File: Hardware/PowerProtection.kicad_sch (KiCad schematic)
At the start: 17 parts, among them IC5 LM76202QPWPRQ1

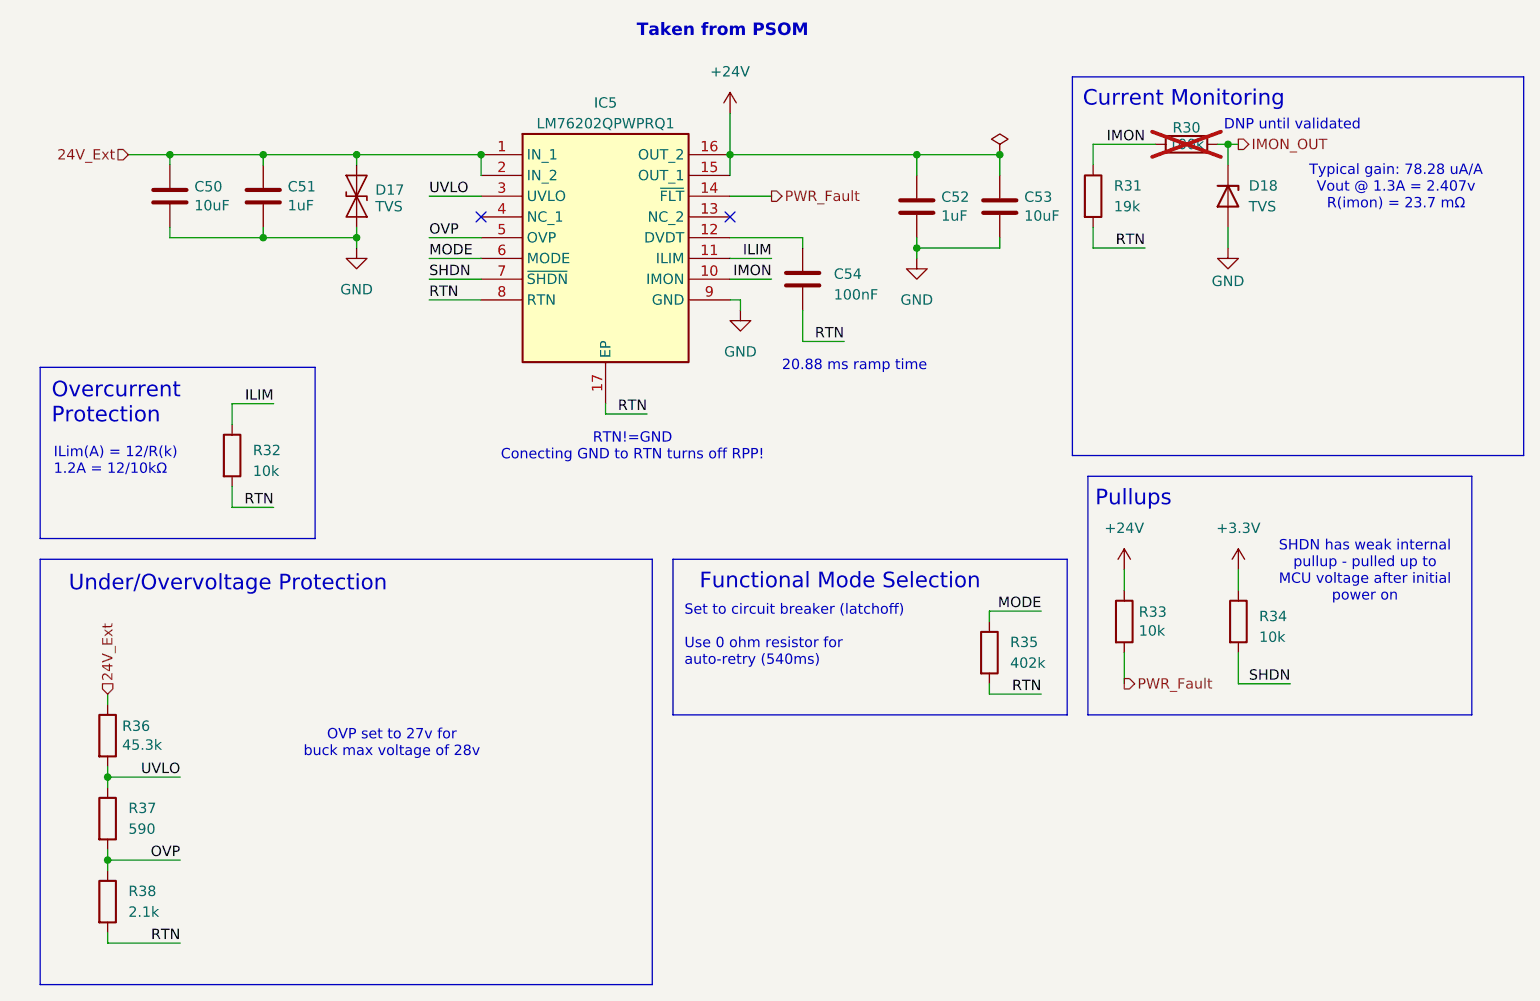
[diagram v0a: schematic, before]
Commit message: RevB Changes (#4)
* added documentation for current range; added VBUS led

* INA common-mode fixed (i think)

* differential amp for LPF

* diff amp / LPF

* some comments so I don't forget what I'm doing

* new TLV symbol, SPDT switch for scrut

* fixed LPF cutoff

* refactored and added LPF docs; added fuse, boot_gpio from USB-UART chip

* i lowk haven't started layout

* slightly cooked

* started layout not really but kind of

* layout stuff

* post review council sch changes: shielded connectors, removed SHDN resistor, diode OR for boot, standardized resistors

* starting routing i think

* almost done with routing

* wow

* drc is happy

* ye

* again

* addressed some comments

* added lcsc part numbers

* generated production files and docs

* updated STEP file

* symbol library

* addressed comments; generated production files, docs

* added Mouser BOM, deleted embedded step files
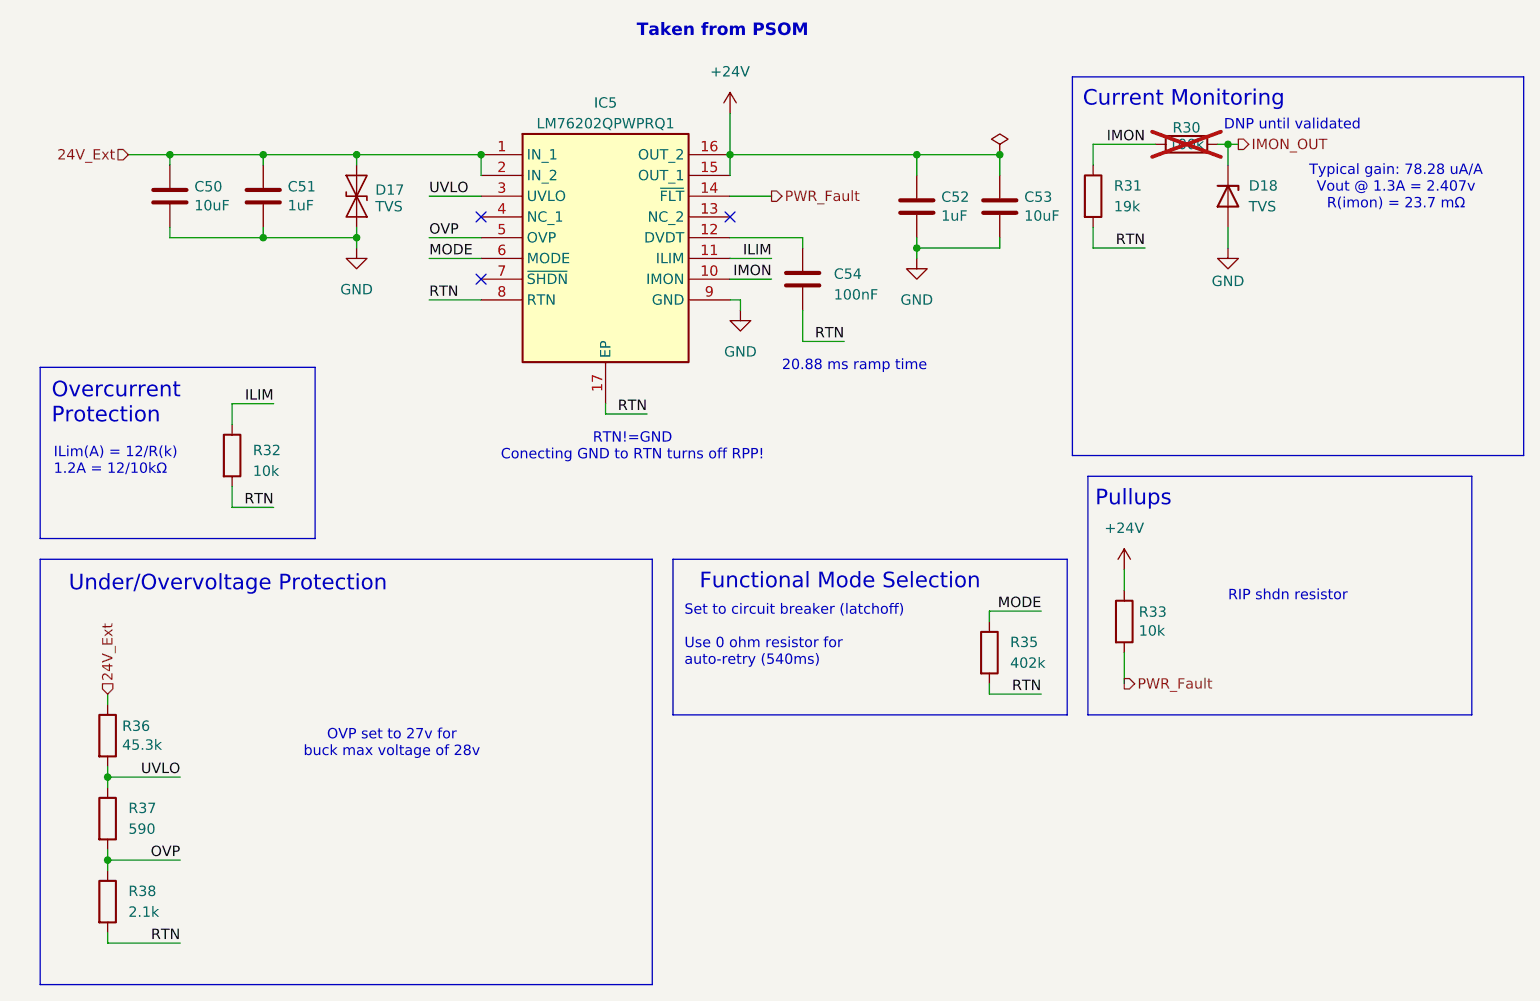
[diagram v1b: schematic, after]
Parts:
- removed R34: 10k, Resistor_SMD:R_0603_1608Metric_Pad0.98x0.95mm_HandSolder, symbol Device:R
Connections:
- net SHDN: no longer names the net of IC5.7 (~{SHDN})
- no-connect marks 2 -> 3
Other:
- note added: "RIP shdn resistor"
- note removed: "SHDN has weak internal pullup - pulled up to MCU voltage after initial power on"
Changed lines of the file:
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@@
 		)
 	)
+	(text "RIP shdn resistor"
+		(exclude_from_sim no)
+		(at 158.75 85.09 0)
+		(effects
+			(font
+				(size 1.27 1.27)
+			)
+			(justify left top)
+		)
+	)
 	(text "Under/Overvoltage Protection"
 		(exclude_from_sim no)
@@
 		)
 	)
-	(text "SHDN has weak internal\npullup - pulled up to\nMCU voltage after initial\npower on"
-		(exclude_from_sim no)
-		(at 175.514 82.804 0)
-		(effects
-			(font
-				(size 1.27 1.27)
-			)
-		)
-	)
 	(text "20.88 ms ramp time"
 		(exclude_from_sim no)
@@
 		(at 67.31 39.37)
 	)
+	(no_connect
+		(at 67.31 46.99)
+	)
 	(wire
 		(pts
@@
 	(wire
 		(pts
-			(xy 160.02 96.52) (xy 160.02 92.71)
-		)
-		(stroke
-			(width 0)
-			(type default)
-		)
-	)
-	(wire
-		(pts
 			(xy 36.83 62.23) (xy 36.83 64.77)
 		)
@@
 	(wire
 		(pts
-			(xy 166.37 96.52) (xy 160.02 96.52)
-		)
-		(stroke
-			(width 0)
-			(type default)
-		)
-	)
-	(wire
-		(pts
 			(xy 52.07 41.91) (xy 52.07 43.18)
 		)
@@
 	(wire
 		(pts
-			(xy 160.02 82.55) (xy 160.02 85.09)
-		)
-		(stroke
-			(width 0)
-			(type default)
-		)
-	)
-	(wire
-		(pts
 			(xy 120.65 43.18) (xy 120.65 44.45)
 		)
@@
 	(wire
 		(pts
-			(xy 60.96 46.99) (xy 67.31 46.99)
-		)
-		(stroke
-			(width 0)
-			(type default)
-		)
-	)
-	(wire
-		(pts
 			(xy 87.63 63.5) (xy 82.55 63.5)
 		)
@@
 		)
 	)
-	(label "SHDN"
-		(at 166.37 96.52 180)
-		(effects
-			(font
-				(size 1.27 1.27)
-			)
-			(justify right bottom)
-		)
-	)
 	(label "IMON"
 		(at 102.87 46.99 180)
@@
 		)
 	)
-	(label "SHDN"
-		(at 60.96 46.99 0)
-		(effects
-			(font
-				(size 1.27 1.27)
-			)
-			(justify left bottom)
-		)
-	)
 	(hierarchical_label "24V_Ext"
 		(shape input)
@@
 	)
 	(symbol
-		(lib_id "power:+3.3V")
-		(at 160.02 82.55 0)
-		(unit 1)
-		(exclude_from_sim no)
-		(in_bom yes)
-		(on_board yes)
-		(dnp no)
-		(fields_autoplaced yes)
-		(property "Reference" "#PWR0124"
-			(at 160.02 86.36 0)
-			(effects
-				(font
-					(size 1.27 1.27)
-				)
-				(hide yes)
-			)
-		)
-		(property "Value" "+3.3V"
-			(at 160.02 77.47 0)
-			(effects
-				(font
-					(size 1.27 1.27)
-				)
-			)
-		)
-		(property "Footprint" ""
-			(at 160.02 82.55 0)
-			(effects
-				(font
-					(size 1.27 1.27)
-				)
-				(hide yes)
-			)
-		)
-		(property "Datasheet" ""
-			(at 160.02 82.55 0)
-			(effects
-				(font
-					(size 1.27 1.27)
-				)
-				(hide yes)
-			)
-		)
-		(property "Description" "Power symbol creates a global label with name \"+3.3V\""
-			(at 160.02 82.55 0)
-			(effects
-				(font
-					(size 1.27 1.27)
-				)
-				(hide yes)
-			)
-		)
-		(pin "1"
-		)
-		(instances
-			(project "BPS-AmperesPCB"
-				(path "/a452d214-ea00-440d-a445-5d6103fda43a/3b2a70f8-48f8-45b9-b0fe-085893d574c0/bd9a5644-5430-4918-ab28-771dd7faeab6"
-					(reference "#PWR0124")
-					(unit 1)
-				)
-			)
-		)
-	)
-	(symbol
 		(lib_id "power:+12V")
 		(at 146.05 82.55 0)
@@
 					(unit 1)
 				)
-			)
-		)
-	)
-	(symbol
-		(lib_id "Device:R")
-		(at 160.02 88.9 0)
-		(unit 1)
-		(exclude_from_sim no)
-		(in_bom yes)
-		(on_board yes)
-		(dnp no)
-		(fields_autoplaced yes)
-		(property "Reference" "R34"
-			(at 162.56 88.265 0)
-			(effects
-				(font
-					(size 1.27 1.27)
-				)
-				(justify left)
-			)
-		)
-		(property "Value" "10k"
-			(at 162.56 90.805 0)
-			(effects
-				(font
-					(size 1.27 1.27)
-				)
-				(justify left)
-			)
-		)
-		(property "Footprint" "Resistor_SMD:R_0603_1608Metric_Pad0.98x0.95mm_HandSolder"
-			(at 158.242 88.9 90)
-			(effects
-				(font
-					(size 1.27 1.27)
-				)
-				(hide yes)
-			)
-		)
-		(property "Datasheet" "~"
-			(at 160.02 88.9 0)
-			(effects
-				(font
-					(size 1.27 1.27)
-				)
-				(hide yes)
-			)
-		)
-		(property "Description" "Resistor"
-			(at 160.02 88.9 0)
-			(effects
-				(font
-					(size 1.27 1.27)
-				)
-				(hide yes)
-			)
-		)
-		(property "P/N" "CRCW060310K0FKEI "
-			(at 160.02 88.9 0)
-			(effects
-				(font
-					(size 1.27 1.27)
-				)
-				(hide yes)
-			)
-		)
-		(property "Mfg" "CRCW060310K0FKEI "
-			(at 160.02 88.9 0)
-			(effects
-				(font
-					(size 1.27 1.27)
-				)
-				(hide yes)
-			)
-		)
-		(pin "1"
-		)
-		(pin "2"
-		)
-		(instances
-			(project "BPS-AmperesPCB"
-				(path "/a452d214-ea00-440d-a445-5d6103fda43a/3b2a70f8-48f8-45b9-b0fe-085893d574c0/bd9a5644-5430-4918-ab28-771dd7faeab6"
-					(reference "R34")
-					(unit 1)
-				)
